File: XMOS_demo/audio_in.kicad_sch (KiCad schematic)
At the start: 0 parts

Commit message: sch mostly finished, needs tp, pcb component layout started
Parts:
- added C57, C62: 470p, Capacitor_SMD:C_0603_1608Metric, symbol Device:C_Small
- added C58, C60: 2n7, Capacitor_SMD:C_0603_1608Metric, symbol Device:C_Small
- added C59, C61: 1u, Capacitor_SMD:CP_Elec_4x5.4, symbol Device:C_Polarized_Small
- added C63, C64, C65: 100n, Capacitor_SMD:C_0603_1608Metric, symbol Device:C_Small
- added J5, J6: AudioJack2_SwitchT, _Connector_Audio:Jack_3.5mm_CUI_MJ-3523-SMT-TR_Horizontal, symbol Connector_Audio:AudioJack2_SwitchT
- added R49, R53: 91R, Resistor_SMD:R_0603_1608Metric, symbol Device:R_Small
- added R50, R54: 634R, Resistor_SMD:R_0603_1608Metric, symbol Device:R_Small
- added R51, R52: 10k, Resistor_SMD:R_0603_1608Metric, symbol Device:R_Small
- added U10, U11, U9: OPA340NA, Package_TO_SOT_SMD:SOT-23-5, symbol Amplifier_Operational:OPA340NA
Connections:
- new net: C62.1, R54.1, U11.4 (-)
- new net: C62.2, R53.1, U11.1
- new net: C57.1, R50.1, U9.4 (-)
- new net: C57.2, R49.1, U9.1
- new net: C61.1, R52.1, U11.3 (+)
- new net: C59.1, R51.2, U9.3 (+)
- new net AIN_A: C58.1, R49.2, R50.2
- new net AIN_B: C60.2, R53.2, R54.2
- new net A_IN_L: C59.2, J5.T
- new net A_IN_R: C61.2, J6.T
- new net GND: C63.2, C64.2, C65.2, J5.S, J6.S, U10.2 (V-), U11.2 (V-), U9.2 (V-)
- new net P5V0: C63.1, C64.1, C65.1, U10.5 (V+), U11.5 (V+), U9.5 (V+)
- new net VQ1: U10.3 (+)
- new net VQ2: C58.2, C60.1, R51.1, R52.2, U10.1, U10.4 (-)
- no-connect marks 0 -> 2

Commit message: finished sch, pcb work
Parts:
- renumbered J5 to J6, J6 to J7, R49 to R47, R50 to R48, R51 to R49, R52 to R50, R53 to R51, R54 to R52
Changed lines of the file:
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@@
 		(on_board yes)
 		(dnp no)
-		(property "Reference" "#PWR087"
+		(property "Reference" "#PWR085"
 			(at 152.4 146.05 0)
 			(effects
@@
 			(project "XMOS_demo"
 				(path "/0a855fb0-ca19-4770-811e-70d8770d7fdd/71bec83b-8ae1-4f4c-8273-5b8329c1423c"
-					(reference "#PWR087")
+					(reference "#PWR085")
 					(unit 1)
 				)
@@
 		(on_board yes)
 		(dnp no)
-		(property "Reference" "R50"
+		(property "Reference" "R48"
 			(at 172.466 72.39 90)
 			(effects
@@
 			(project "XMOS_demo"
 				(path "/0a855fb0-ca19-4770-811e-70d8770d7fdd/71bec83b-8ae1-4f4c-8273-5b8329c1423c"
-					(reference "R50")
+					(reference "R48")
 					(unit 1)
 				)
@@
 		(on_board yes)
 		(dnp no)
-		(property "Reference" "R49"
+		(property "Reference" "R47"
 			(at 172.466 49.53 90)
 			(effects
@@
 			(project "XMOS_demo"
 				(path "/0a855fb0-ca19-4770-811e-70d8770d7fdd/71bec83b-8ae1-4f4c-8273-5b8329c1423c"
-					(reference "R49")
+					(reference "R47")
 					(unit 1)
 				)
@@
 		(on_board yes)
 		(dnp no)
-		(property "Reference" "#PWR089"
+		(property "Reference" "#PWR087"
 			(at 119.38 161.29 0)
 			(effects
@@
 			(project "XMOS_demo"
 				(path "/0a855fb0-ca19-4770-811e-70d8770d7fdd/71bec83b-8ae1-4f4c-8273-5b8329c1423c"
-					(reference "#PWR089")
+					(reference "#PWR087")
 					(unit 1)
 				)
@@
 		(on_board yes)
 		(dnp no)
-		(property "Reference" "#PWR086"
+		(property "Reference" "#PWR084"
 			(at 114.3 140.97 0)
 			(effects
@@
 			(project "XMOS_demo"
 				(path "/0a855fb0-ca19-4770-811e-70d8770d7fdd/71bec83b-8ae1-4f4c-8273-5b8329c1423c"
-					(reference "#PWR086")
+					(reference "#PWR084")
 					(unit 1)
 				)
@@
 		(on_board yes)
 		(dnp no)
-		(property "Reference" "#PWR083"
+		(property "Reference" "#PWR080"
 			(at 114.3 97.79 0)
 			(effects
@@
 			(project "XMOS_demo"
 				(path "/0a855fb0-ca19-4770-811e-70d8770d7fdd/71bec83b-8ae1-4f4c-8273-5b8329c1423c"
-					(reference "#PWR083")
+					(reference "#PWR080")
 					(unit 1)
 				)
@@
 		(on_board yes)
 		(dnp no)
-		(property "Reference" "#PWR091"
+		(property "Reference" "#PWR089"
 			(at 109.22 173.99 0)
 			(effects
@@
 			(project "XMOS_demo"
 				(path "/0a855fb0-ca19-4770-811e-70d8770d7fdd/71bec83b-8ae1-4f4c-8273-5b8329c1423c"
-					(reference "#PWR091")
+					(reference "#PWR089")
 					(unit 1)
 				)
@@
 		(on_board yes)
 		(dnp no)
-		(property "Reference" "R52"
+		(property "Reference" "R50"
 			(at 141.478 108.458 0)
 			(effects
@@
 			(project "XMOS_demo"
 				(path "/0a855fb0-ca19-4770-811e-70d8770d7fdd/71bec83b-8ae1-4f4c-8273-5b8329c1423c"
-					(reference "R52")
+					(reference "R50")
 					(unit 1)
 				)
@@
 		(on_board yes)
 		(dnp no)
-		(property "Reference" "#PWR084"
+		(property "Reference" "#PWR082"
 			(at 175.26 118.11 0)
 			(effects
@@
 			(project "XMOS_demo"
 				(path "/0a855fb0-ca19-4770-811e-70d8770d7fdd/71bec83b-8ae1-4f4c-8273-5b8329c1423c"
-					(reference "#PWR084")
+					(reference "#PWR082")
 					(unit 1)
 				)
@@
 		(on_board yes)
 		(dnp no)
-		(property "Reference" "#PWR080"
+		(property "Reference" "#PWR078"
 			(at 152.4 46.99 0)
 			(effects
@@
 			(project "XMOS_demo"
 				(path "/0a855fb0-ca19-4770-811e-70d8770d7fdd/71bec83b-8ae1-4f4c-8273-5b8329c1423c"
-					(reference "#PWR080")
+					(reference "#PWR078")
 					(unit 1)
 				)
@@
 		(on_board yes)
 		(dnp no)
-		(property "Reference" "#PWR088"
+		(property "Reference" "#PWR086"
 			(at 109.22 161.29 0)
 			(effects
@@
 			(project "XMOS_demo"
 				(path "/0a855fb0-ca19-4770-811e-70d8770d7fdd/71bec83b-8ae1-4f4c-8273-5b8329c1423c"
-					(reference "#PWR088")
+					(reference "#PWR086")
 					(unit 1)
 				)
@@
 		(on_board yes)
 		(dnp no)
-		(property "Reference" "J5"
+		(property "Reference" "J6"
 			(at 107.696 77.216 0)
 			(effects
@@
 			(project "XMOS_demo"
 				(path "/0a855fb0-ca19-4770-811e-70d8770d7fdd/71bec83b-8ae1-4f4c-8273-5b8329c1423c"
-					(reference "J5")
+					(reference "J6")
 					(unit 1)
 				)
@@
 		(on_board yes)
 		(dnp no)
-		(property "Reference" "#PWR081"
+		(property "Reference" "#PWR079"
 			(at 152.4 69.85 0)
 			(effects
@@
 			(project "XMOS_demo"
 				(path "/0a855fb0-ca19-4770-811e-70d8770d7fdd/71bec83b-8ae1-4f4c-8273-5b8329c1423c"
-					(reference "#PWR081")
+					(reference "#PWR079")
 					(unit 1)
 				)
@@
 		(on_board yes)
 		(dnp no)
-		(property "Reference" "R51"
+		(property "Reference" "R49"
 			(at 141.224 92.964 0)
 			(effects
@@
 			(project "XMOS_demo"
 				(path "/0a855fb0-ca19-4770-811e-70d8770d7fdd/71bec83b-8ae1-4f4c-8273-5b8329c1423c"
-					(reference "R51")
+					(reference "R49")
 					(unit 1)
 				)
@@
 		(on_board yes)
 		(dnp no)
-		(property "Reference" "#PWR082"
+		(property "Reference" "#PWR081"
 			(at 175.26 95.25 0)
 			(effects
@@
 			(project "XMOS_demo"
 				(path "/0a855fb0-ca19-4770-811e-70d8770d7fdd/71bec83b-8ae1-4f4c-8273-5b8329c1423c"
-					(reference "#PWR082")
+					(reference "#PWR081")
 					(unit 1)
 				)
@@
 		(on_board yes)
 		(dnp no)
-		(property "Reference" "#PWR092"
+		(property "Reference" "#PWR090"
 			(at 119.38 173.99 0)
 			(effects
@@
 			(project "XMOS_demo"
 				(path "/0a855fb0-ca19-4770-811e-70d8770d7fdd/71bec83b-8ae1-4f4c-8273-5b8329c1423c"
-					(reference "#PWR092")
+					(reference "#PWR090")
 					(unit 1)
 				)
@@
 		(on_board yes)
 		(dnp no)
-		(property "Reference" "R54"
+		(property "Reference" "R52"
 			(at 169.926 151.13 90)
 			(effects
@@
 			(project "XMOS_demo"
 				(path "/0a855fb0-ca19-4770-811e-70d8770d7fdd/71bec83b-8ae1-4f4c-8273-5b8329c1423c"
-					(reference "R54")
+					(reference "R52")
 					(unit 1)
 				)
@@
 		(on_board yes)
 		(dnp no)
-		(property "Reference" "#PWR090"
+		(property "Reference" "#PWR088"
 			(at 129.54 161.29 0)
 			(effects
@@
 			(project "XMOS_demo"
 				(path "/0a855fb0-ca19-4770-811e-70d8770d7fdd/71bec83b-8ae1-4f4c-8273-5b8329c1423c"
-					(reference "#PWR090")
+					(reference "#PWR088")
 					(unit 1)
 				)
@@
 		(on_board yes)
 		(dnp no)
-		(property "Reference" "R53"
+		(property "Reference" "R51"
 			(at 172.466 125.73 90)
 			(effects
@@
 			(project "XMOS_demo"
 				(path "/0a855fb0-ca19-4770-811e-70d8770d7fdd/71bec83b-8ae1-4f4c-8273-5b8329c1423c"
-					(reference "R53")
+					(reference "R51")
 					(unit 1)
 				)
@@
 		(on_board yes)
 		(dnp no)
-		(property "Reference" "#PWR085"
+		(property "Reference" "#PWR083"
 			(at 152.4 123.19 0)
 			(effects
@@
 			(project "XMOS_demo"
 				(path "/0a855fb0-ca19-4770-811e-70d8770d7fdd/71bec83b-8ae1-4f4c-8273-5b8329c1423c"
-					(reference "#PWR085")
+					(reference "#PWR083")
 					(unit 1)
 				)
@@
 		(on_board yes)
 		(dnp no)
-		(property "Reference" "#PWR093"
+		(property "Reference" "#PWR091"
 			(at 129.54 173.99 0)
 			(effects
@@
 			(project "XMOS_demo"
 				(path "/0a855fb0-ca19-4770-811e-70d8770d7fdd/71bec83b-8ae1-4f4c-8273-5b8329c1423c"
-					(reference "#PWR093")
+					(reference "#PWR091")
 					(unit 1)
 				)
@@
 		(on_board yes)
 		(dnp no)
-		(property "Reference" "J6"
+		(property "Reference" "J7"
 			(at 107.696 120.396 0)
 			(effects
@@
 			(project "XMOS_demo"
 				(path "/0a855fb0-ca19-4770-811e-70d8770d7fdd/71bec83b-8ae1-4f4c-8273-5b8329c1423c"
-					(reference "J6")
-					(unit 1)
-				)
+					(reference "J7")
+					(unit 1)
+				)

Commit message: pcb routing
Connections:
- net VQ2 renamed VQ2_3
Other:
- company: (none) -> AGH University
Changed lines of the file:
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@@
 	(generator_version "9.0")
 	(paper "A4")
+	(title_block
+		(date "2026-03-29")
+		(rev "0.1")
+		(company "AGH University")
+	)
 	(junction
 		(at 144.78 127)
@@
 	(junction
 		(at 167.64 129.54)
-		(diameter 0)
-		(color 0 0 0 0)
-	)
-	(junction
-		(at 185.42 119.38)
 		(diameter 0)
 		(color 0 0 0 0)
@@
 		(pts
 			(xy 119.38 165.1) (xy 119.38 167.64)
-		)
-		(stroke
-			(width 0)
-			(type default)
-		)
-	)
-	(wire
-		(pts
-			(xy 185.42 119.38) (xy 193.04 119.38)
 		)
 		(stroke
@@
 		)
 	)
-	(hierarchical_label "VQ2"
+	(hierarchical_label "VQ2_3"
 		(shape output)
 		(at 193.04 83.82 0)
 		(effects
 			(font
-				(size 1.27 1.27)
-			)
-			(justify left)
-		)
-	)
-	(hierarchical_label "VQ3"
-		(shape output)
-		(at 193.04 119.38 0)
-		(effects
-			(font

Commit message: I2S config sch page added
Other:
- title: (none) -> USB Sound Card Audio Input
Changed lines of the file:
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@@
 	(paper "A4")
 	(title_block
+		(title "USB Sound Card Audio Input")
 		(date "2026-03-29")
 		(rev "0.1")

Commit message: Summary (required)
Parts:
- renumbered C57 to C65, C58 to C66, C59 to C67, C60 to C68, C61 to C69, C62 to C70, C63 to C71, C64 to C72, C65 to C73, J6 to J8, J7 to J9, R47 to R54, R48 to R55, R49 to R56, R50 to R57, R51 to R58, R52 to R59

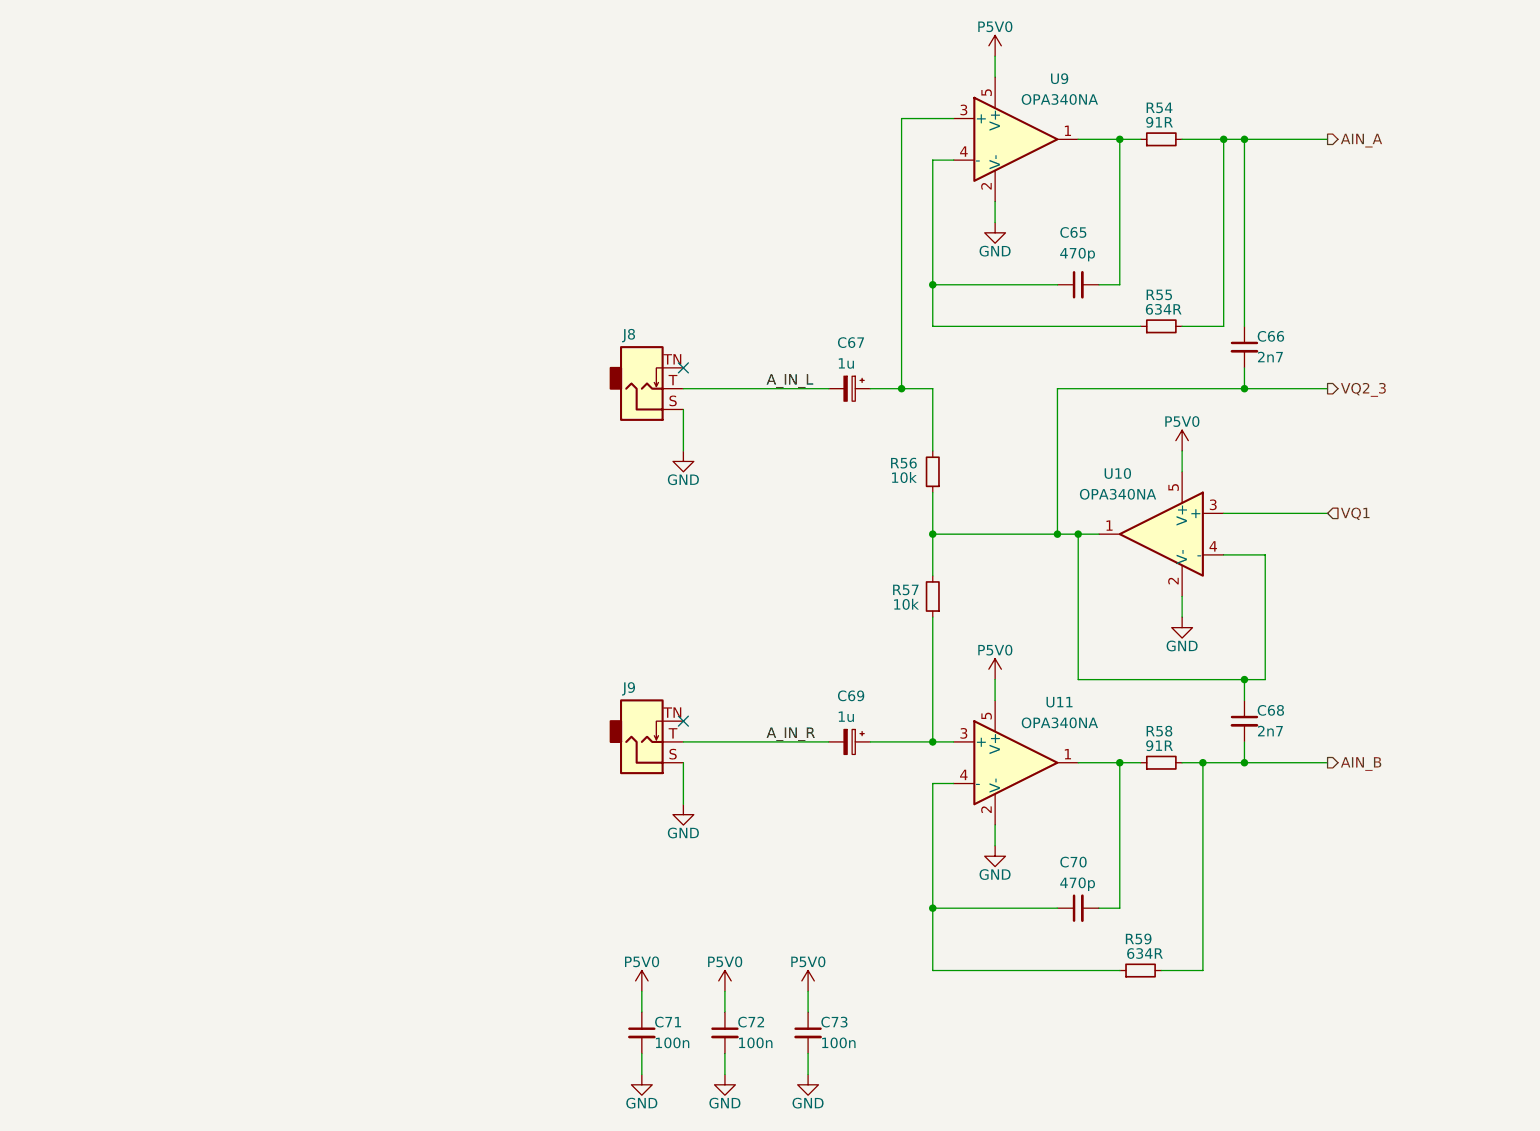
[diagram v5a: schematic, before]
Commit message: Started changes on power supply (audio in) on schematic
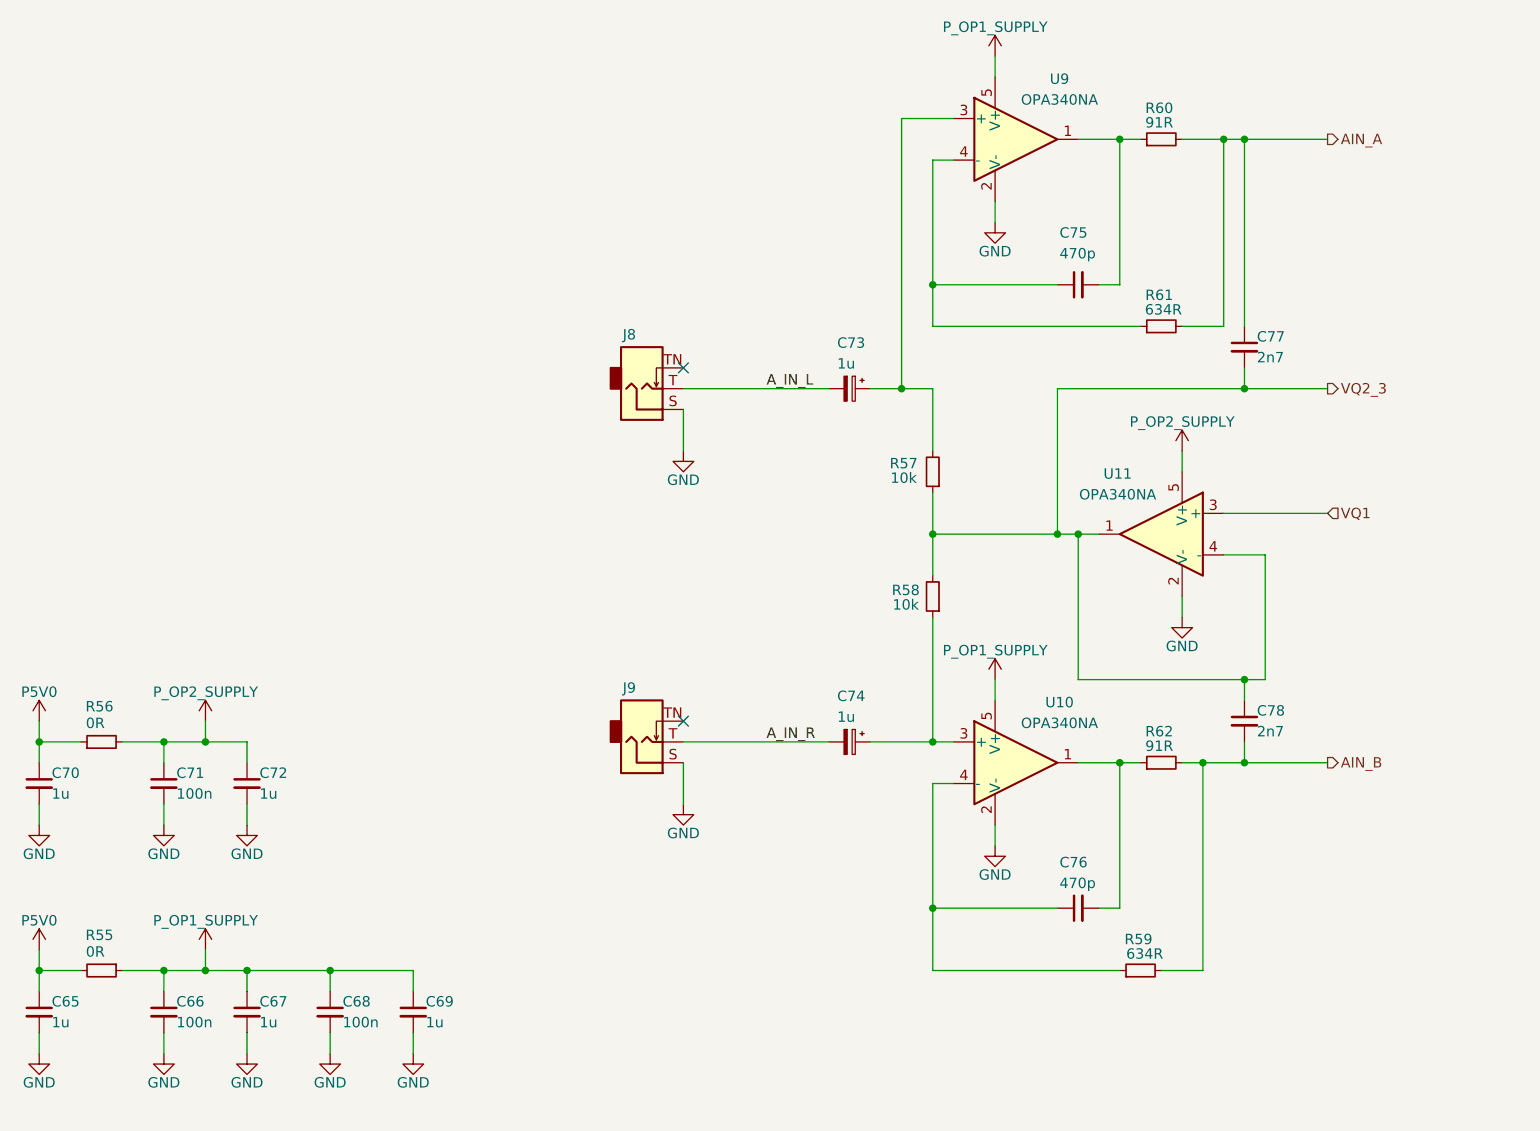
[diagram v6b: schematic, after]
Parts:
- added C65, C67, C69, C70, C72: 1u, Capacitor_SMD:C_0603_1608Metric, symbol Device:C_Small
- added R55, R56: 0R, Resistor_SMD:R_0603_1608Metric, symbol Device:R_Small
- renumbered C71 to C66, C72 to C68, C73 to C71, C67 to C73, C69 to C74, C65 to C75, C70 to C76, C66 to C77, C68 to C78, R56 to R57, R57 to R58, R54 to R60, R55 to R61, R58 to R62, U11 to U10, U10 to U11
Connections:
- net GND: now also C65.2, C67.2, C69.2, C70.2, C72.2
- net P5V0: now also C65.1, C70.1, R55.2, R56.1; no longer C66.1, C68.1, C71.1, U10.5 (V+), U11.5 (V+), U9.5 (V+)
- new net P_OP1_SUPPLY: C66.1, C67.1, C68.1, C69.1, R55.1, U10.5 (V+), U9.5 (V+)
- new net P_OP2_SUPPLY: C71.1, C72.1, R56.2, U11.5 (V+)
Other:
- moved on the sheet: C66, C68, C71

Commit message: Passive lpf added to autio output
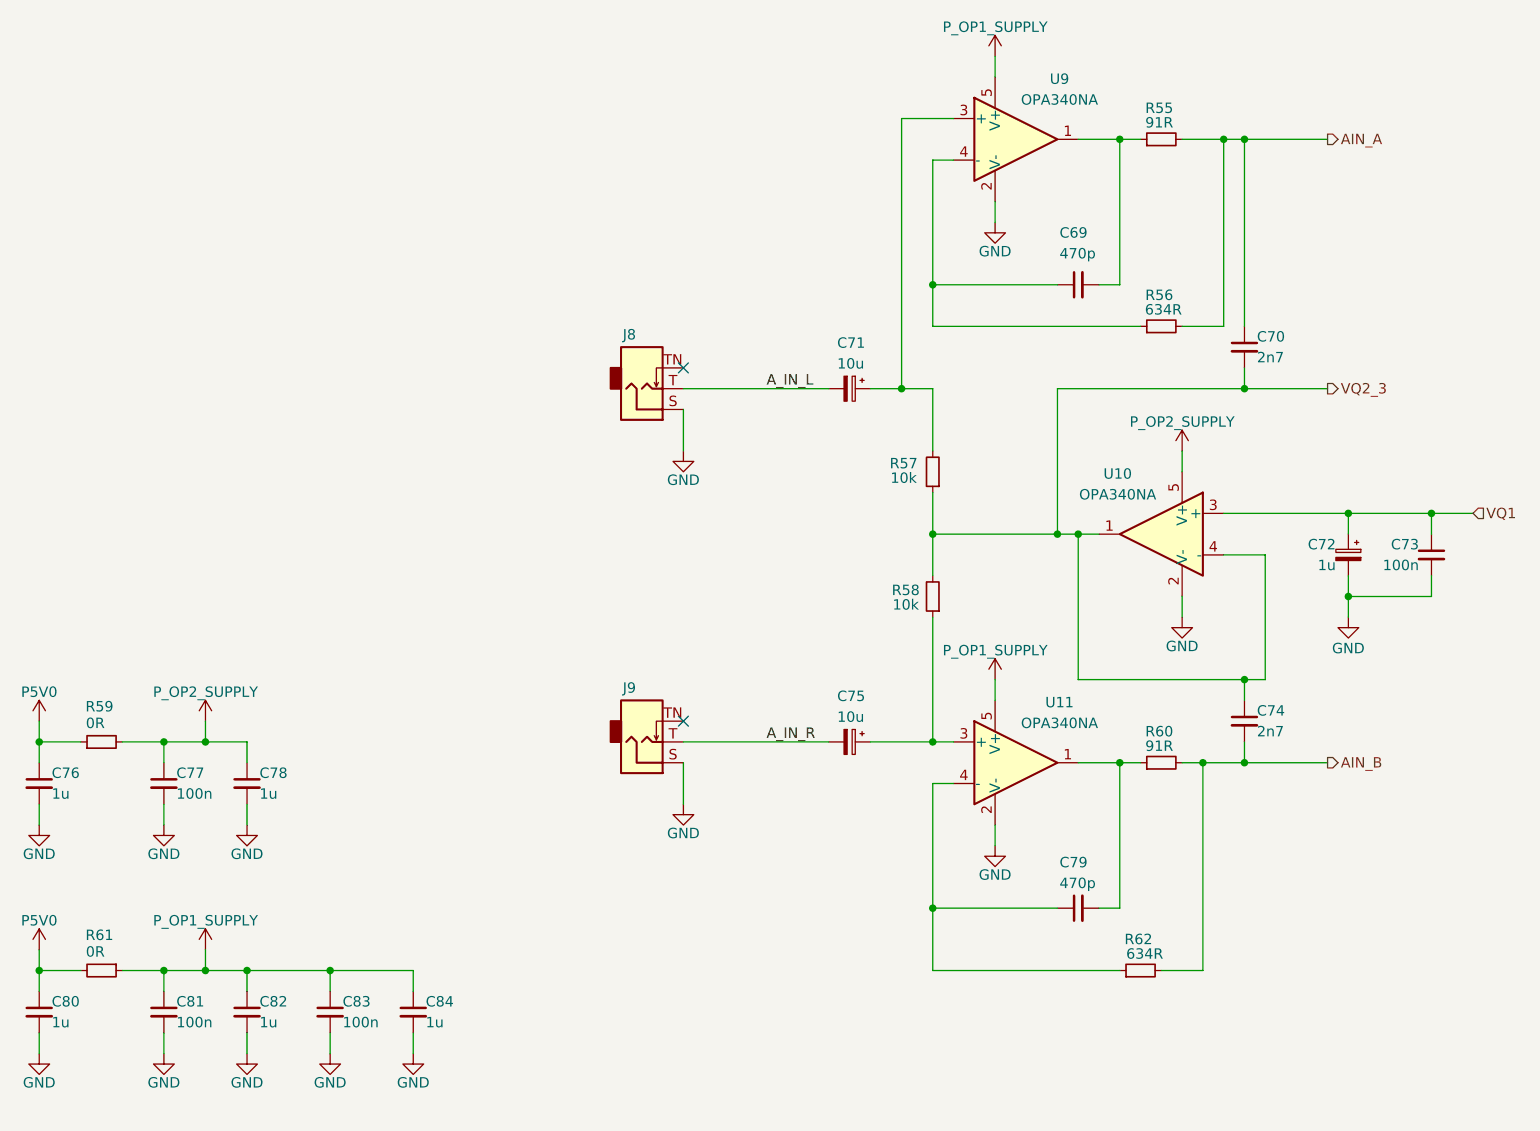
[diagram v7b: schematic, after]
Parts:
- added C72: 1u, Capacitor_SMD:CP_Elec_4x5.4, symbol Device:C_Polarized_Small
- added C73: 100n, Capacitor_SMD:C_0603_1608Metric, symbol Device:C_Small
- C71: renamed from C73; value 1u -> 10u
- C75: renamed from C74; value 1u -> 10u
- renumbered C75 to C69, C77 to C70, C78 to C74, C70 to C76, C71 to C77, C72 to C78, C76 to C79, C65 to C80, C66 to C81, C67 to C82, C68 to C83, C69 to C84, R60 to R55, R61 to R56, R56 to R59, R62 to R60, R55 to R61, R59 to R62, U11 to U10, U10 to U11
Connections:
- net GND: now also C72.2, C73.2
- net VQ1: now also C72.1, C73.1

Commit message: PCB work
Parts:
- renumbered C69 to C71, C70 to C72, C71 to C73, C72 to C74, C73 to C75, C74 to C76, C75 to C77, C76 to C78, C77 to C79, C78 to C80, C79 to C81, C80 to C82, C81 to C83, C82 to C84, C83 to C85, C84 to C86
